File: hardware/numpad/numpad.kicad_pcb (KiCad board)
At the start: 2 copper layers, 0 parts

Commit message: key field placed, outline and mounting holes
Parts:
- added C1: 10u, Capacitor_SMD:C_0805_2012Metric, F.Cu at (186.6, 128.2)
- added C10: 100n, Capacitor_SMD:C_0603_1608Metric, F.Cu at (191.7, 94.1)
- added C11: 1u, Capacitor_SMD:C_0603_1608Metric, F.Cu at (191.7, 96.6)
- added C12: 100n, Capacitor_SMD:C_0603_1608Metric, F.Cu at (191.7, 99.1)
- added C13: 100n, Capacitor_SMD:C_0603_1608Metric, F.Cu at (195.7, 89.1)
- added C14: 100n, Capacitor_SMD:C_0603_1608Metric, F.Cu at (195.7, 91.6)
- added C15: 27p, Capacitor_SMD:C_0603_1608Metric, F.Cu at (195.7, 94.1)
- added C16: 27p, Capacitor_SMD:C_0603_1608Metric, F.Cu at (195.7, 96.6)
- added C17: 100n, Capacitor_SMD:C_0603_1608Metric, F.Cu at (203.1, 56.8)
- added C18: 100n, Capacitor_SMD:C_0603_1608Metric, F.Cu at (203.1, 59.3)
- added C19: 100n, Capacitor_SMD:C_0603_1608Metric, F.Cu at (203.1, 61.8)
- added C2: 10u, Capacitor_SMD:C_0805_2012Metric, F.Cu at (186.6, 131.2)
- added C20: 100n, Capacitor_SMD:C_0603_1608Metric, F.Cu at (203.1, 64.3)
- added C21: 100n, Capacitor_SMD:C_0603_1608Metric, F.Cu at (203.1, 66.8)
- added C22: 100n, Capacitor_SMD:C_0603_1608Metric, F.Cu at (203.1, 69.3)
- added C23: 100n, Capacitor_SMD:C_0603_1608Metric, F.Cu at (203.1, 71.8)
- added C24: 100n, Capacitor_SMD:C_0603_1608Metric, F.Cu at (207.1, 56.8)
- added C25: 100n, Capacitor_SMD:C_0603_1608Metric, F.Cu at (207.1, 59.3)
- added C26: 100n, Capacitor_SMD:C_0603_1608Metric, F.Cu at (207.1, 61.8)
- added C27: 100n, Capacitor_SMD:C_0603_1608Metric, F.Cu at (207.1, 64.3)
- added C28: 100n, Capacitor_SMD:C_0603_1608Metric, F.Cu at (207.1, 66.8)
- added C29: 100n, Capacitor_SMD:C_0603_1608Metric, F.Cu at (207.1, 69.3)
- added C3: 1u, Capacitor_SMD:C_0603_1608Metric, F.Cu at (187.7, 89.1)
- added C30: 100n, Capacitor_SMD:C_0603_1608Metric, F.Cu at (207.1, 71.8)
- added C31: 100n, Capacitor_SMD:C_0603_1608Metric, F.Cu at (211.1, 56.8)
- added C32: 100n, Capacitor_SMD:C_0603_1608Metric, F.Cu at (211.1, 59.3)
- added C33: 100n, Capacitor_SMD:C_0603_1608Metric, F.Cu at (211.1, 61.8)
- added C34: 100n, Capacitor_SMD:C_0603_1608Metric, F.Cu at (211.1, 64.3)
- added C35: 22u, Capacitor_SMD:C_0805_2012Metric, F.Cu at (203.3, 74.6)
- added C36: 22u, Capacitor_SMD:C_0805_2012Metric, F.Cu at (203.3, 77.6)
- added C4: 100n, Capacitor_SMD:C_0603_1608Metric, F.Cu at (187.7, 91.6)
- added C5: 100n, Capacitor_SMD:C_0603_1608Metric, F.Cu at (187.7, 94.1)
- added C6: 100n, Capacitor_SMD:C_0603_1608Metric, F.Cu at (187.7, 96.6)
- added C7: 100n, Capacitor_SMD:C_0603_1608Metric, F.Cu at (187.7, 99.1)
- added C8: 100n, Capacitor_SMD:C_0603_1608Metric, F.Cu at (191.7, 89.1)
- added C9: 100n, Capacitor_SMD:C_0603_1608Metric, F.Cu at (191.7, 91.6)
- added D1: 1N4148W, Diode_SMD:D_SOD-123, F.Cu at (156.9, 57.2)
- added D10: 1N4148W, Diode_SMD:D_SOD-123, F.Cu at (162.7, 63.9)
- added D11: 1N4148W, Diode_SMD:D_SOD-123, F.Cu at (162.7, 67.2)
- added D12: 1N4148W, Diode_SMD:D_SOD-123, F.Cu at (162.7, 70.6)
- added D13: 1N4148W, Diode_SMD:D_SOD-123, F.Cu at (162.7, 73.9)
- added D14: 1N4148W, Diode_SMD:D_SOD-123, F.Cu at (162.7, 77.3)
- added D15: 1N4148W, Diode_SMD:D_SOD-123, F.Cu at (168.5, 57.2)
- added D16: 1N4148W, Diode_SMD:D_SOD-123, F.Cu at (168.5, 60.5)
- added D17: 1N4148W, Diode_SMD:D_SOD-123, F.Cu at (168.5, 63.9)
- added D18: 1N4148W, Diode_SMD:D_SOD-123, F.Cu at (168.5, 67.2)
- added D2: 1N4148W, Diode_SMD:D_SOD-123, F.Cu at (156.9, 60.5)
- added D3: 1N4148W, Diode_SMD:D_SOD-123, F.Cu at (156.9, 63.9)
- added D4: 1N4148W, Diode_SMD:D_SOD-123, F.Cu at (156.9, 67.2)
- added D5: 1N4148W, Diode_SMD:D_SOD-123, F.Cu at (156.9, 70.6)
- added D6: 1N4148W, Diode_SMD:D_SOD-123, F.Cu at (156.9, 73.9)
- added D7: 1N4148W, Diode_SMD:D_SOD-123, F.Cu at (156.9, 77.3)
- added D8: 1N4148W, Diode_SMD:D_SOD-123, F.Cu at (162.7, 57.2)
- added D9: 1N4148W, Diode_SMD:D_SOD-123, F.Cu at (162.7, 60.5)
- added J1: USB_C_Receptacle_USB2.0_16P, Connector_USB:USB_C_Receptacle_HRO_TYPE-C-31-M-12, F.Cu at (180.3, 122.0)
- added J2: Conn_01x03, Connector_PinHeader_2.54mm:PinHeader_1x03_P2.54mm_Vertical, F.Cu at (187.9, 102.6)
- added J3: Conn_01x04, Connector_PinHeader_2.54mm:PinHeader_1x04_P2.54mm_Vertical, F.Cu at (195.6, 118.5)
- added LED1: MX_SK6812MINI-E, PCM_marbastlib-mx:LED_MX_6028R, B.Cu at (60.0, 40.0)
- added LED10: MX_SK6812MINI-E, PCM_marbastlib-mx:LED_MX_6028R, B.Cu at (79.0, 78.1)
- added LED11: MX_SK6812MINI-E, PCM_marbastlib-mx:LED_MX_6028R, B.Cu at (98.1, 78.1)
- added LED12: MX_SK6812MINI-E, PCM_marbastlib-mx:LED_MX_6028R, B.Cu at (60.0, 97.2)
- added LED13: MX_SK6812MINI-E, PCM_marbastlib-mx:LED_MX_6028R, B.Cu at (79.0, 97.2)
- added LED14: MX_SK6812MINI-E, PCM_marbastlib-mx:LED_MX_6028R, B.Cu at (98.1, 97.2)
- added LED15: MX_SK6812MINI-E, PCM_marbastlib-mx:LED_MX_6028R, B.Cu at (69.5, 116.2)
- added LED16: MX_SK6812MINI-E, PCM_marbastlib-mx:LED_MX_6028R, B.Cu at (98.1, 116.2)
- added LED17: MX_SK6812MINI-E, PCM_marbastlib-mx:LED_MX_6028R, B.Cu at (117.2, 106.7)
- added LED2: MX_SK6812MINI-E, PCM_marbastlib-mx:LED_MX_6028R, B.Cu at (79.0, 40.0)
- added LED3: MX_SK6812MINI-E, PCM_marbastlib-mx:LED_MX_6028R, B.Cu at (98.1, 40.0)
- added LED4: MX_SK6812MINI-E, PCM_marbastlib-mx:LED_MX_6028R, B.Cu at (117.2, 40.0)
- added LED5: MX_SK6812MINI-E, PCM_marbastlib-mx:LED_MX_6028R, B.Cu at (60.0, 59.0)
- added LED6: MX_SK6812MINI-E, PCM_marbastlib-mx:LED_MX_6028R, B.Cu at (79.0, 59.0)
- added LED7: MX_SK6812MINI-E, PCM_marbastlib-mx:LED_MX_6028R, B.Cu at (98.1, 59.0)
- added LED8: MX_SK6812MINI-E, PCM_marbastlib-mx:LED_MX_6028R, B.Cu at (117.2, 68.6)
- added LED9: MX_SK6812MINI-E, PCM_marbastlib-mx:LED_MX_6028R, B.Cu at (60.0, 78.1)
- added MX1: NUM, PCM_marbastlib-mx:SW_MX_HS_CPG151101S11_1u, B.Cu at (60.0, 40.0)
- added MX10: 5, PCM_marbastlib-mx:SW_MX_HS_CPG151101S11_1u, B.Cu at (79.0, 78.1)
- added MX11: 6, PCM_marbastlib-mx:SW_MX_HS_CPG151101S11_1u, B.Cu at (98.1, 78.1)
- added MX12: 1, PCM_marbastlib-mx:SW_MX_HS_CPG151101S11_1u, B.Cu at (60.0, 97.2)
- added MX13: 2, PCM_marbastlib-mx:SW_MX_HS_CPG151101S11_1u, B.Cu at (79.0, 97.2)
- added MX14: 3, PCM_marbastlib-mx:SW_MX_HS_CPG151101S11_1u, B.Cu at (98.1, 97.2)
- added MX15: 0, PCM_marbastlib-mx:SW_MX_HS_CPG151101S11_1u, B.Cu at (69.5, 116.2)
- added MX16: PERIOD, PCM_marbastlib-mx:SW_MX_HS_CPG151101S11_1u, B.Cu at (98.1, 116.2)
- added MX17: ENTER, PCM_marbastlib-mx:SW_MX_HS_CPG151101S11_1u, B.Cu at (117.2, 106.7)
- added MX2: DIV, PCM_marbastlib-mx:SW_MX_HS_CPG151101S11_1u, B.Cu at (79.0, 40.0)
- added MX3: MULT, PCM_marbastlib-mx:SW_MX_HS_CPG151101S11_1u, B.Cu at (98.1, 40.0)
- added MX4: MIN, PCM_marbastlib-mx:SW_MX_HS_CPG151101S11_1u, B.Cu at (117.2, 40.0)
- added MX5: 7, PCM_marbastlib-mx:SW_MX_HS_CPG151101S11_1u, B.Cu at (60.0, 59.0)
- added MX6: 8, PCM_marbastlib-mx:SW_MX_HS_CPG151101S11_1u, B.Cu at (79.0, 59.0)
- added MX7: 9, PCM_marbastlib-mx:SW_MX_HS_CPG151101S11_1u, B.Cu at (98.1, 59.0)
- added MX8: PLUS, PCM_marbastlib-mx:SW_MX_HS_CPG151101S11_1u, B.Cu at (117.2, 68.6)
- added MX9: 4, PCM_marbastlib-mx:SW_MX_HS_CPG151101S11_1u, B.Cu at (60.0, 78.1)
- added Q1: BSS138, Package_TO_SOT_SMD:SOT-23, F.Cu at (200.4, 118.4)
- added Q2: BSS138, Package_TO_SOT_SMD:SOT-23, F.Cu at (200.4, 122.9)
- added R1: 5k1, Resistor_SMD:R_0603_1608Metric, F.Cu at (188.2, 122.1)
- added R10: 4k7, Resistor_SMD:R_0603_1608Metric, F.Cu at (204.8, 117.5)
- added R11: 4k7, Resistor_SMD:R_0603_1608Metric, F.Cu at (204.8, 120.0)
- added R2: 5k1, Resistor_SMD:R_0603_1608Metric, F.Cu at (188.2, 124.6)
- added R3: 10k, Resistor_SMD:R_0603_1608Metric, F.Cu at (195.7, 99.1)
- added R4: 10k, Resistor_SMD:R_0603_1608Metric, F.Cu at (199.7, 89.1)
- added R5: 1k, Resistor_SMD:R_0603_1608Metric, F.Cu at (199.7, 91.6)
- added R6: 27, Resistor_SMD:R_0603_1608Metric, F.Cu at (199.7, 94.1)
- added R7: 27, Resistor_SMD:R_0603_1608Metric, F.Cu at (199.7, 96.6)
- added R8: 1k, Resistor_SMD:R_0603_1608Metric, F.Cu at (199.7, 99.1)
- added R9: 470, Resistor_SMD:R_0603_1608Metric, F.Cu at (211.1, 66.8)
- added REF**: STAB_MX_2u, PCM_marbastlib-mx:STAB_MX_2u, B.Cu at (117.2, 68.6)
- added REF**: STAB_MX_2u, PCM_marbastlib-mx:STAB_MX_2u, B.Cu at (117.2, 106.7)
- added REF**: STAB_MX_2u, PCM_marbastlib-mx:STAB_MX_2u, B.Cu at (69.5, 116.2)
- added SW1: BOOTSEL, Button_Switch_SMD:SW_SPST_PTS645Sx43SMTR92, F.Cu at (180.1, 91.7)
- added SW2: RESET, Button_Switch_SMD:SW_SPST_PTS645Sx43SMTR92, F.Cu at (180.1, 99.6)
- added SW3: RotaryEncoder_Switch, Rotary_Encoder:RotaryEncoder_Alps_EC11E-Switch_Vertical_H20mm, F.Cu at (156.0, 84.1)
- added U1: NCP1117-3.3_SOT223, Package_TO_SOT_SMD:SOT-223-3_TabPin2, F.Cu at (179.4, 130.9)
- added U2: USBLC6-2SC6, Package_TO_SOT_SMD:SOT-23-6, F.Cu at (188.8, 118.6)
- added U3: RP2040, Package_DFN_QFN:QFN-56-1EP_7x7mm_P0.4mm_EP3.2x3.2mm, F.Cu at (195.3, 105.0)
- added U4: W25Q128JVS, Package_SO:SOIC-8_5.3x5.3mm_P1.27mm, F.Cu at (179.7, 107.0)
- added U5: 74AHCT1G125, Package_TO_SOT_SMD:SOT-23-5, F.Cu at (208.1, 75.5)
- added Y1: 12MHz, Crystal:Crystal_SMD_3225-4Pin_3.2x2.5mm, F.Cu at (192.9, 111.9)
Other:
- board outline added: 83 x 124 mm

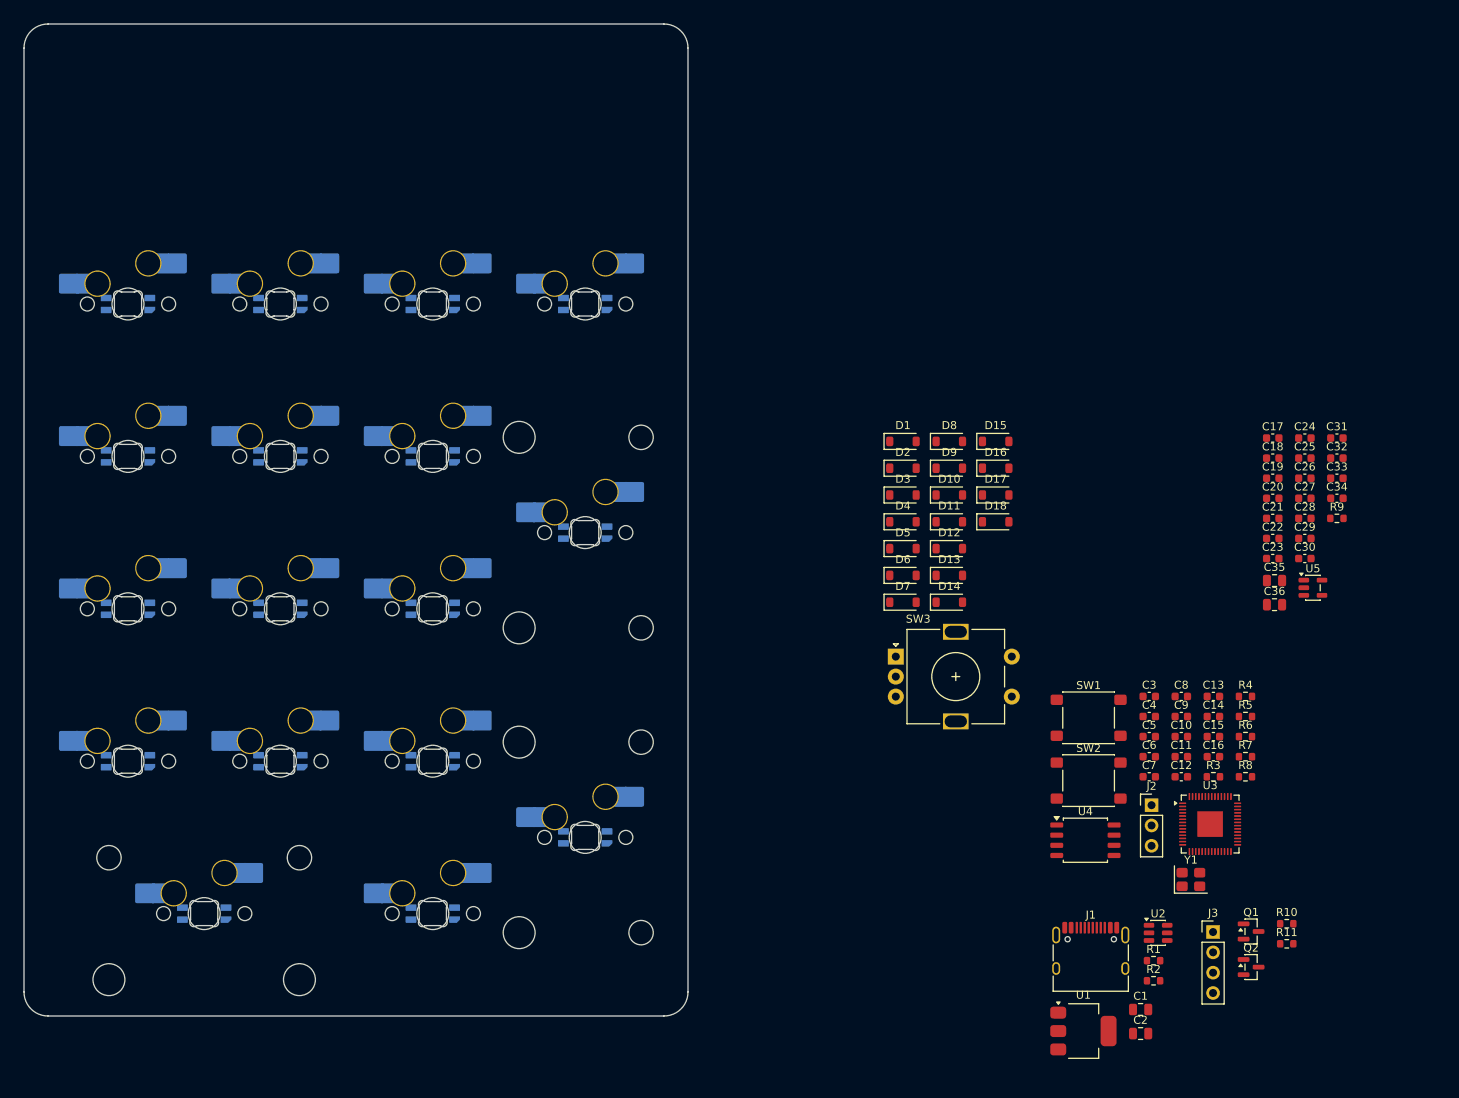
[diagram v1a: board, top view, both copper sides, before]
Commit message: add key field diodes and LED caps
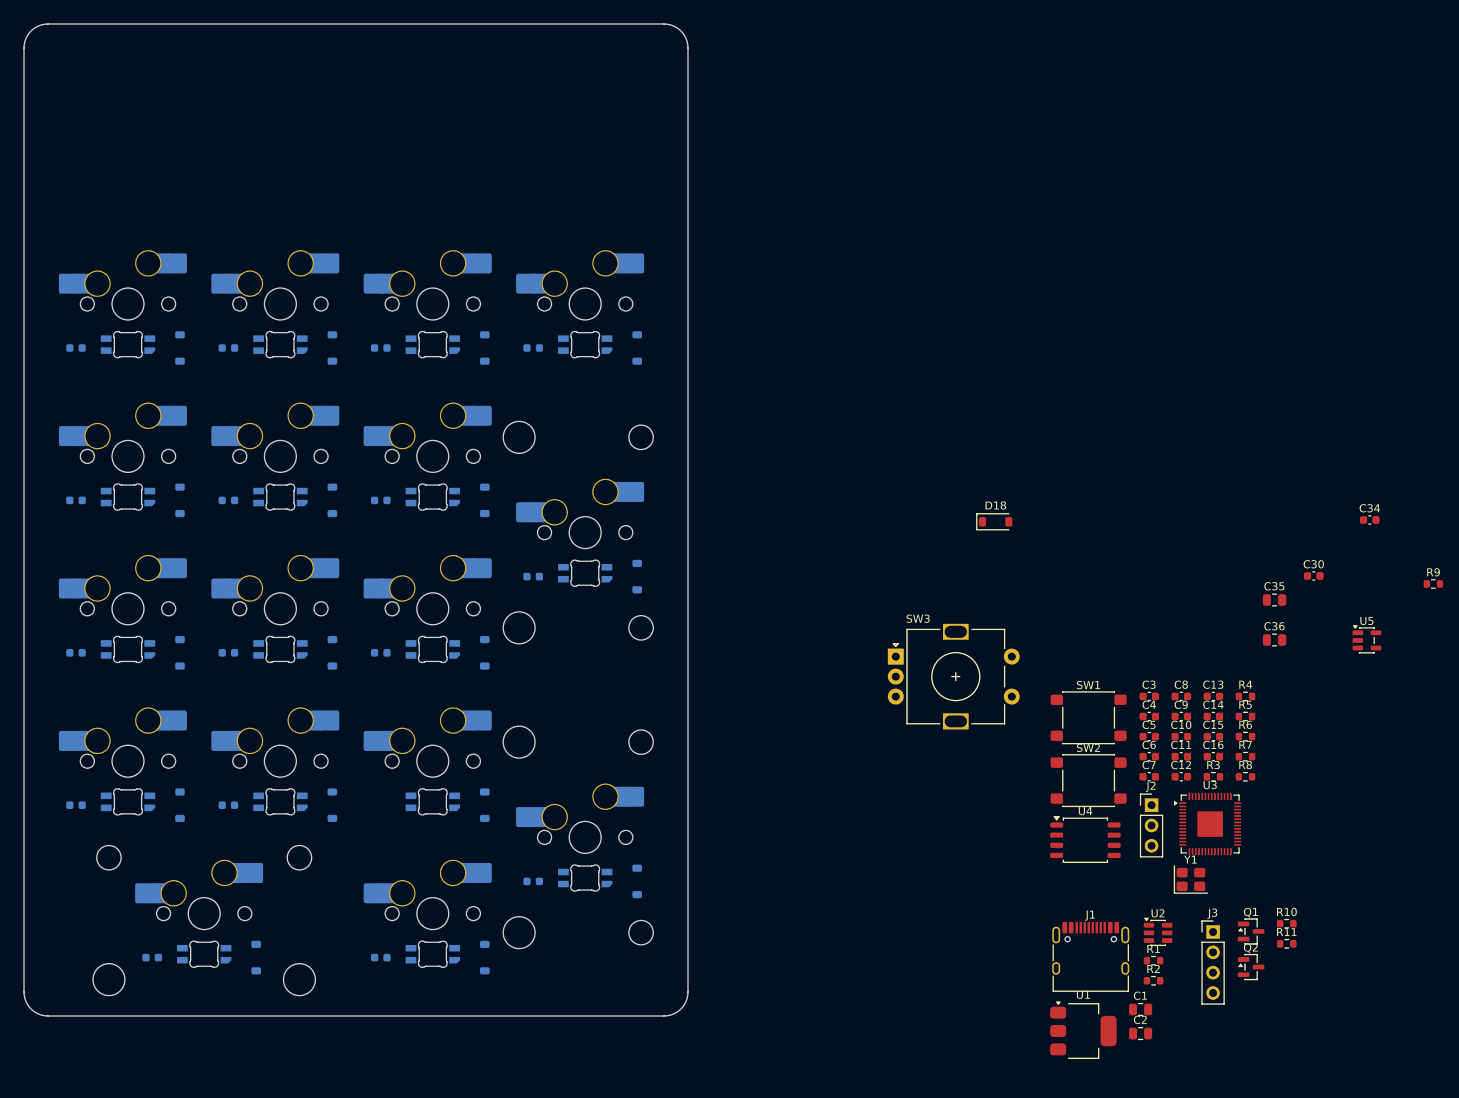
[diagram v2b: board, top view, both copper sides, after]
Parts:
- C17, C18, C19, C20, C21, C22, C23, C24, C25, C26, C27, C28, C29, C31, C32, C33, D1, D10, D11, D12, D13, D14, D15, D16, D17, D2, D3, D4, D5, D6, D7, D8, D9: moved to B.Cu
- moved C31 161.7 mm to (63.0, 121.7), turned to 180 degrees
- moved C28 157.7 mm to (53.5, 102.7), turned to 180 degrees
- moved C25 155.5 mm to (53.5, 83.6), turned to 180 degrees
- moved C17 150.0 mm to (53.5, 45.5), turned to 180 degrees
- moved C21 149.6 mm to (53.5, 64.5), turned to 180 degrees
- moved C29 138.6 mm to (72.5, 102.7), turned to 180 degrees
- moved C26 136.3 mm to (72.5, 83.6), turned to 180 degrees
- moved C32 134.8 mm to (91.6, 121.7), turned to 180 degrees
- moved C18 131.3 mm to (72.5, 45.5), turned to 180 degrees
- moved C22 130.6 mm to (72.5, 64.5), turned to 180 degrees
- moved C27 117.1 mm to (91.6, 83.6), turned to 180 degrees
- moved D15 112.7 mm to (76.0, 121.7), turned to 90 degrees
- moved C19 112.7 mm to (91.6, 45.5), turned to 180 degrees
- moved C33 112.4 mm to (110.7, 112.2), turned to 180 degrees
- moved C23 111.7 mm to (91.6, 64.5), turned to 180 degrees
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
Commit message: USB entry and MCU cluster
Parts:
- C11, C3: value 1u -> 100n
- moved C1 172.2 mm to (59.5, 12.0), turned to 90 degrees
- moved C2 166.1 mm to (66.0, 17.0)
- moved U1 165.0 mm to (66.0, 11.0)
- moved Y1 152.5 mm to (66.5, 26.5)
- moved R1 148.7 mm to (84.5, 15.5), turned to 90 degrees
- moved C15 147.6 mm to (63.0, 29.3)
- moved C14 146.5 mm to (66.5, 22.5)
- moved C13 146.1 mm to (66.5, 20.8)
- moved J1 145.9 mm to (88.5, 8.65), turned to 180 degrees
- moved U3 145.6 mm to (74.0, 24.4)
- moved R2 145.1 mm to (92.5, 15.5), turned to 90 degrees
- moved C16 144.8 mm to (67.5, 29.3)
- moved U2 142.9 mm to (88.5, 16.8)
- moved C11 140.8 mm to (74.0, 19.3)
- moved U4 138.7 mm to (75.5, 15.5)
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
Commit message: MCU cluster complete
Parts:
- moved R4 148.8 mm to (75.5, 11.0)
- moved R6 139.5 mm to (84.0, 20.0), turned to 90 degrees
- moved R7 139.1 mm to (86.0, 20.0), turned to 90 degrees
- moved R9 17.6 mm to (206.0, 79.0)
- moved C35 8.00 mm to (203.3, 69.0)
- moved C36 8.00 mm to (203.3, 74.0)
- moved C34 7.50 mm to (208.0, 69.0)
- moved U5 3.61 mm to (212.9, 85.0)
- moved R8 1.91 mm to (202.2, 101.0)
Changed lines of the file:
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@@
 	)
 	(footprint "Package_DFN_QFN:QFN-56-1EP_7x7mm_P0.4mm_EP3.2x3.2mm"
+		(locked yes)
 		(layer "F.Cu")
 		(at 74 24.4)
@@
 	)
 	(footprint "Resistor_SMD:R_0603_1608Metric"
+		(locked yes)
 		(layer "F.Cu")
-		(at 202.175 94.075)
+		(at 84 20 90)
 		(descr "Resistor SMD 0603 (1608 Metric), square (rectangular) end terminal, IPC-7351 nominal, (Body size source: IPC-SM-782 page 72, https://www.pcb-3d.com/wordpress/wp-content/uploads/ipc-sm-782a_amendment_1_and_2.pdf)")
 		(tags "resistor")
 		(property "Reference" "R6"
-			(at 0 -1.43 0)
+			(at 0 -1.43 90)
 			(layer "F.SilkS")
 			(effects
@@
 		)
 		(property "Value" "27"
-			(at 0 1.43 0)
+			(at 0 1.43 90)
 			(layer "F.Fab")
 			(effects
@@
 		)
 		(property "Datasheet" ""
-			(at 0 0 0)
+			(at 0 0 90)
 			(layer "F.Fab")
 			(hide yes)
@@
 		)
 		(property "Description" "Resistor"
-			(at 0 0 0)
+			(at 0 0 90)
 			(layer "F.Fab")
 			(hide yes)
@@
 		)
 		(property "KiLib_Generator" "SMD_2terminal_chip_molded"
-			(at 0 0 0)
+			(at 0 0 90)
 			(layer "F.SilkS")
 			(hide yes)
@@
 		)
 		(fp_text user "${REFERENCE}"
-			(at 0 0 0)
+			(at 0 0 90)
 			(layer "F.Fab")
 			(effects
@@
 		)
 		(pad "1" smd roundrect
-			(at -0.825 0)
+			(at -0.825 0 90)
 			(size 0.8 0.95)
 			(layers "F.Cu" "F.Mask" "F.Paste")
@@
 		)
 		(pad "2" smd roundrect
-			(at 0.825 0)
+			(at 0.825 0 90)
 			(size 0.8 0.95)
 			(layers "F.Cu" "F.Mask" "F.Paste")
@@
 	)
 	(footprint "Capacitor_SMD:C_0603_1608Metric"
+		(locked yes)
 		(layer "F.Cu")
 		(at 67.5 29.3)
@@
 	(footprint "Capacitor_SMD:C_0805_2012Metric"
 		(layer "F.Cu")
-		(at 203.315 77)
+		(at 203.315 69)
 		(descr "Capacitor SMD 0805 (2012 Metric), square (rectangular) end terminal, IPC-7351 nominal, (Body size source: IPC-SM-782 page 76, https://www.pcb-3d.com/wordpress/wp-content/uploads/ipc-sm-782a_amendment_1_and_2.pdf, https://docs.google.com/spreadsheets/d/1BsfQQcO9C6DZCsRaXUlFlo91Tg2WpOkGARC1WS5S8t0/edit?usp=sharing)")
 		(tags "capacitor")
@@
 	)
 	(footprint "Capacitor_SMD:C_0603_1608Metric"
+		(locked yes)
 		(layer "F.Cu")
 		(at 71.5 29.5)
@@
 	)
 	(footprint "Resistor_SMD:R_0603_1608Metric"
+		(locked yes)
 		(layer "F.Cu")
-		(at 202.175 89.055)
+		(at 75.5 11)
 		(descr "Resistor SMD 0603 (1608 Metric), square (rectangular) end terminal, IPC-7351 nominal, (Body size source: IPC-SM-782 page 72, https://www.pcb-3d.com/wordpress/wp-content/uploads/ipc-sm-782a_amendment_1_and_2.pdf)")
 		(tags "resistor")
@@
 	)
 	(footprint "Capacitor_SMD:C_0603_1608Metric"
+		(locked yes)
 		(layer "F.Cu")
 		(at 77 19.3)
@@
 	)
 	(footprint "Capacitor_SMD:C_0603_1608Metric"
+		(locked yes)
 		(layer "F.Cu")
 		(at 79 22.5 90)
@@
 	(footprint "Package_TO_SOT_SMD:SOT-23-5"
 		(layer "F.Cu")
-		(at 214.8625 82.05)
+		(at 212.8625 85.05)
 		(descr "SOT, 5 Pin (JEDEC MO-178 Var AA https://www.jedec.org/document_search?search_api_views_fulltext=MO-178)")
 		(tags "SOT TO_SOT_SMD")
@@
 	)
 	(footprint "Capacitor_SMD:C_0603_1608Metric"
+		(locked yes)
 		(layer "F.Cu")
 		(at 66.5 22.5)
@@
 	)
 	(footprint "Rotary_Encoder:RotaryEncoder_Alps_EC11E-Switch_Vertical_H20mm"
+		(locked yes)
 		(layer "F.Cu")
 		(at 110.5 15.5)
@@
 	)
 	(footprint "Capacitor_SMD:C_0603_1608Metric"
+		(locked yes)
 		(layer "F.Cu")
 		(at 71 19.3)
@@
 	)
 	(footprint "Resistor_SMD:R_0603_1608Metric"
+		(locked yes)
 		(layer "F.Cu")
-		(at 202.175 96.585)
+		(at 86 20 90)
 		(descr "Resistor SMD 0603 (1608 Metric), square (rectangular) end terminal, IPC-7351 nominal, (Body size source: IPC-SM-782 page 72, https://www.pcb-3d.com/wordpress/wp-content/uploads/ipc-sm-782a_amendment_1_and_2.pdf)")
 		(tags "resistor")
 		(property "Reference" "R7"
-			(at 0 -1.43 0)
+			(at 0 -1.43 90)
 			(layer "F.SilkS")
 			(effects
@@
 		)
 		(property "Value" "27"
-			(at 0 1.43 0)
+			(at 0 1.43 90)
 			(layer "F.Fab")
 			(effects
@@
 		)
 		(property "Datasheet" ""
-			(at 0 0 0)
+			(at 0 0 90)
 			(layer "F.Fab")
 			(hide yes)
@@
 		)
 		(property "Description" "Resistor"
-			(at 0 0 0)
+			(at 0 0 90)
 			(layer "F.Fab")
 			(hide yes)
@@
 		)
 		(property "KiLib_Generator" "SMD_2terminal_chip_molded"
-			(at 0 0 0)
+			(at 0 0 90)
 			(layer "F.SilkS")
 			(hide yes)
@@
 		)
 		(fp_text user "${REFERENCE}"
-			(at 0 0 0)
+			(at 0 0 90)
 			(layer "F.Fab")
 			(effects
@@
 		)
 		(pad "1" smd roundrect
-			(at -0.825 0)
+			(at -0.825 0 90)
 			(size 0.8 0.95)
 			(layers "F.Cu" "F.Mask" "F.Paste")
@@
 		)
 		(pad "2" smd roundrect
-			(at 0.825 0)
+			(at 0.825 0 90)
 			(size 0.8 0.95)
 			(layers "F.Cu" "F.Mask" "F.Paste")
@@
 	)
 	(footprint "Crystal:Crystal_SMD_3225-4Pin_3.2x2.5mm"
+		(locked yes)
 		(layer "F.Cu")
 		(at 66.5 26.5)
@@
 	(footprint "Resistor_SMD:R_0603_1608Metric"
 		(layer "F.Cu")
-		(at 202.175 99.095)
+		(at 202.175 101)
 		(descr "Resistor SMD 0603 (1608 Metric), square (rectangular) end terminal, IPC-7351 nominal, (Body size source: IPC-SM-782 page 72, https://www.pcb-3d.com/wordpress/wp-content/uploads/ipc-sm-782a_amendment_1_and_2.pdf)")
 		(tags "resistor")
@@
 	)
 	(footprint "Capacitor_SMD:C_0603_1608Metric"
+		(locked yes)
 		(layer "F.Cu")
 		(at 79 25.5 90)
@@
 	)
 	(footprint "Capacitor_SMD:C_0603_1608Metric"
+		(locked yes)
 		(layer "F.Cu")
 		(at 77.5 29.5)
@@
 	(footprint "Capacitor_SMD:C_0603_1608Metric"
 		(layer "F.Cu")
-		(at 215.225 67)
+		(at 208 69)
 		(descr "Capacitor SMD 0603 (1608 Metric), square (rectangular) end terminal, IPC-7351 nominal, (Body size source: IPC-SM-782 page 76, https://www.pcb-3d.com/wordpress/wp-content/uploads/ipc-sm-782a_amendment_1_and_2.pdf)")
 		(tags "capacitor")
@@
 	)
 	(footprint "Package_SO:SOIC-8_5.3x5.3mm_P1.27mm"
+		(locked yes)
 		(layer "F.Cu")
 		(at 75.5 15.5)
@@
 	)
 	(footprint "Capacitor_SMD:C_0603_1608Metric"
+		(locked yes)
 		(layer "F.Cu")
 		(at 63 29.3)
@@
 	)
 	(footprint "Capacitor_SMD:C_0603_1608Metric"
+		(locked yes)
 		(layer "F.Cu")
 		(at 74 19.3)
@@
 	)
 	(footprint "Capacitor_SMD:C_0603_1608Metric"
+		(locked yes)
 		(layer "F.Cu")
 		(at 79 28 90)
@@
 	)
 	(footprint "Capacitor_SMD:C_0603_1608Metric"
+		(locked yes)
 		(layer "F.Cu")
 		(at 74.5 29.5)
@@
 	)
 	(footprint "Capacitor_SMD:C_0603_1608Metric"
+		(locked yes)
 		(layer "F.Cu")
 		(at 66.5 20.8)
@@
 	)
 	(footprint "Capacitor_SMD:C_0603_1608Metric"
+		(locked yes)
 		(layer "F.Cu")
 		(at 81.5 15.5 90)
@@
 	(footprint "Resistor_SMD:R_0603_1608Metric"
 		(layer "F.Cu")
-		(at 223.175 75)
+		(at 206 79)
 		(descr "Resistor SMD 0603 (1608 Metric), square (rectangular) end terminal, IPC-7351 nominal, (Body size source: IPC-SM-782 page 72, https://www.pcb-3d.com/wordpress/wp-content/uploads/ipc-sm-782a_amendment_1_and_2.pdf)")
 		(tags "resistor")
@@
 	(footprint "Capacitor_SMD:C_0805_2012Metric"
 		(layer "F.Cu")
-		(at 203.315 82)
+		(at 203.315 74)
 		(descr "Capacitor SMD 0805 (2012 Metric), square (rectangular) end terminal, IPC-7351 nominal, (Body size source: IPC-SM-782 page 76, https://www.pcb-3d.com/wordpress/wp-content/uploads/ipc-sm-782a_amendment_1_and_2.pdf, https://docs.google.com/spreadsheets/d/1BsfQQcO9C6DZCsRaXUlFlo91Tg2WpOkGARC1WS5S8t0/edit?usp=sharing)")
 		(tags "capacitor")

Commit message: RGB spine, placement complete
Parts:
- C34, C35, C36, R9, U5: moved to B.Cu
- moved U5 165.3 mm to (57.0, 30.0), turned to 180 degrees
- moved C34 159.3 mm to (53.5, 30.0), turned to 180 degrees
- moved C36 157.8 mm to (49.0, 41.0), turned to 90 degrees
- moved C35 157.6 mm to (49.0, 37.0), turned to 90 degrees
- moved R9 153.1 mm to (60.0, 33.0), turned to 90 degrees
- moved R5 130.0 mm to (96.0, 16.5)
- moved R8 126.5 mm to (108.0, 16.5)
- moved J2 108.4 mm to (120.0, 13.0), turned to 90 degrees
- moved SW2 106.9 mm to (108.0, 12.0)
- moved SW1 104.6 mm to (96.0, 12.0)
- moved R10 79.5 mm to (157.0, 54.7)
- moved R11 79.5 mm to (158.0, 60.7)
- moved J3 79.5 mm to (142.0, 61.9)
- moved Q1 79.5 mm to (150.9, 57.8)
- moved Q2 79.5 mm to (151.0, 66.7)
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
